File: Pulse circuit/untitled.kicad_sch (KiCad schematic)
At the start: 1 part, among them U4 MP1584EN(SOIC8E)

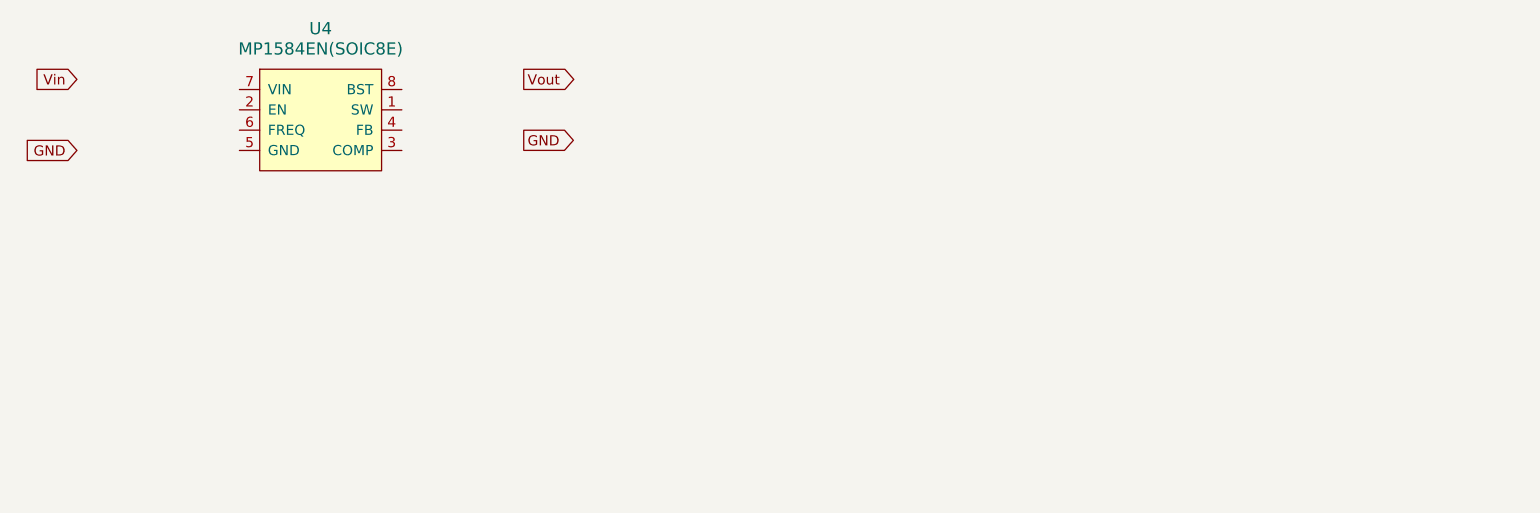
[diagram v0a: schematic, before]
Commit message: schematic of buck converter
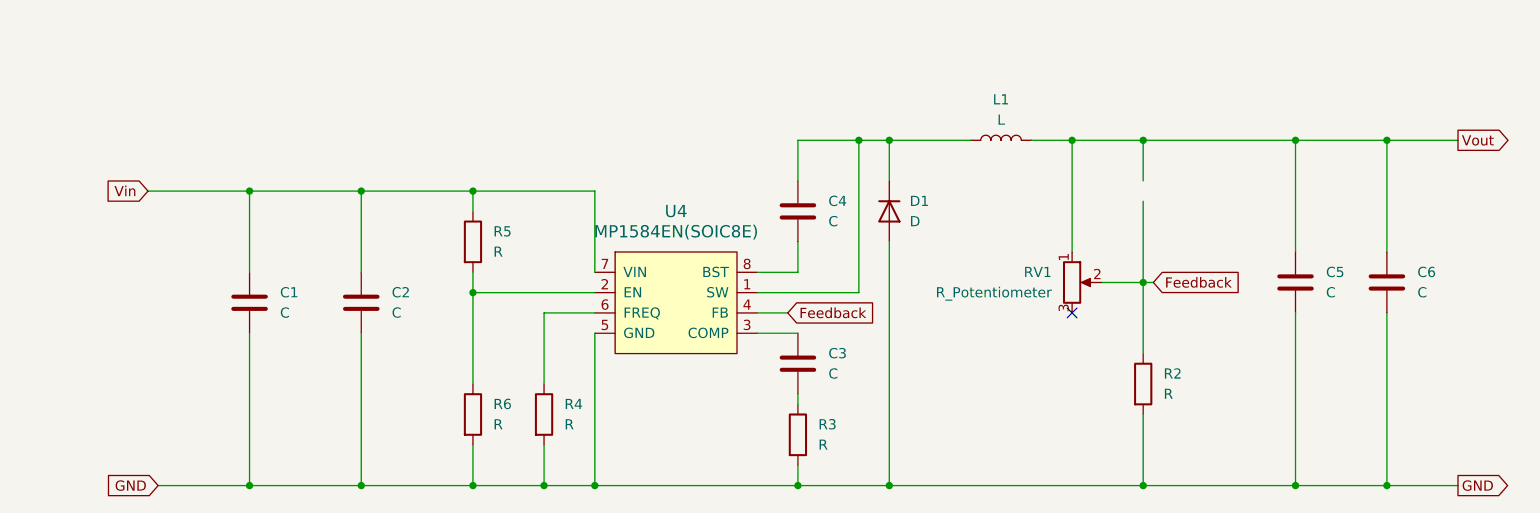
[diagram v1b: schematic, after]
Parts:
- added C1, C2, C3, C4, C5, C6: C, symbol Device:C
- added D1: D, symbol Device:D
- added L1: L, symbol Device:L
- added R2, R3, R4, R5, R6: R, symbol Device:R
- added RV1: R_Potentiometer, symbol Device:R_Potentiometer
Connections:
- net GND: now also U4.5 (GND), U4.EP, U4.EP1 (EP@1), C1.2, C2.2, C5.2, C6.2, D1.2 (A), R2.2, R3.2, R4.2, R6.2
- net Vin: now also U4.7 (VIN), C1.1, C2.1, R5.1
- net Vout: now also C5.1, C6.1, L1.2, RV1.1
- net at U4.1 (SW): now also C4.1, D1.1 (K), L1.1
- net at U4.2 (EN): now also R5.2, R6.1
- net at U4.3 (COMP): now also C3.1
- net Feedback: now reaches U4.4 (FB)
- net Feedback: now also R2.1, RV1.2
- net at U4.6 (FREQ): now also R4.1
- net at U4.8 (BST): now also C4.2
- new net: C3.2, R3.1
- no-connect marks 0 -> 1
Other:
- moved on the sheet: U4

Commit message: Changed the annotations
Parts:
- D1: value D -> ~
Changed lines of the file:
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@@
 			)
 		)
-		(property "Value" "D"
+		(property "Value" "~"
 			(at 162.56 77.4699 90)
 			(effects

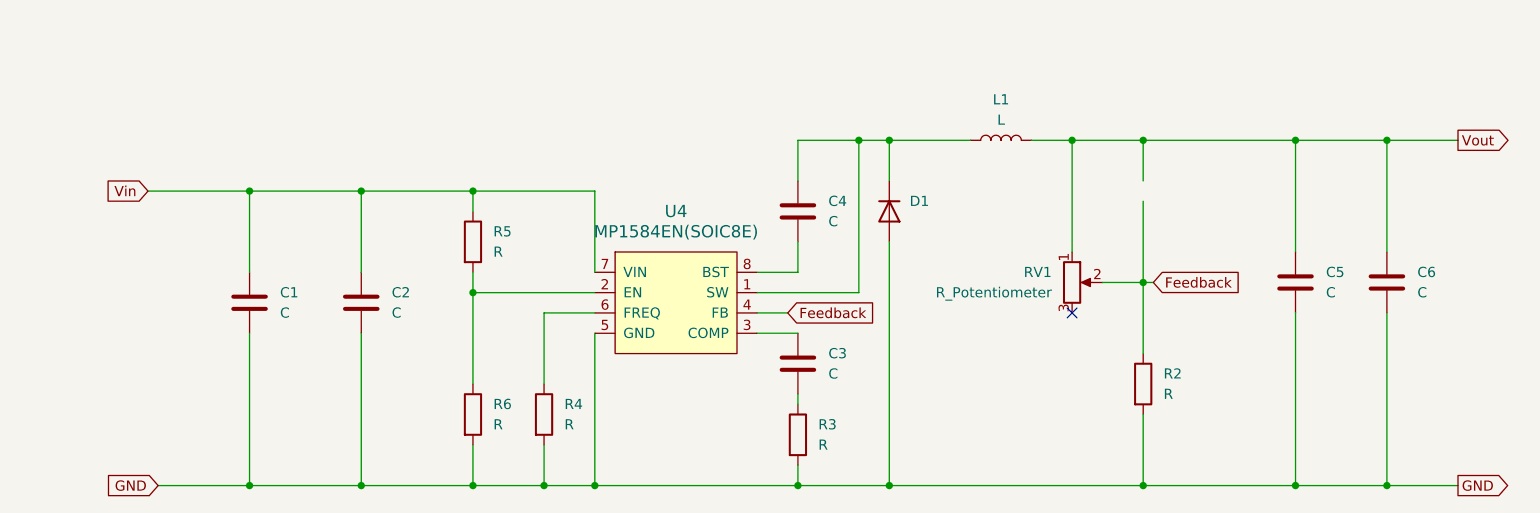
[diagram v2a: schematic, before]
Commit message: values added to buck converter
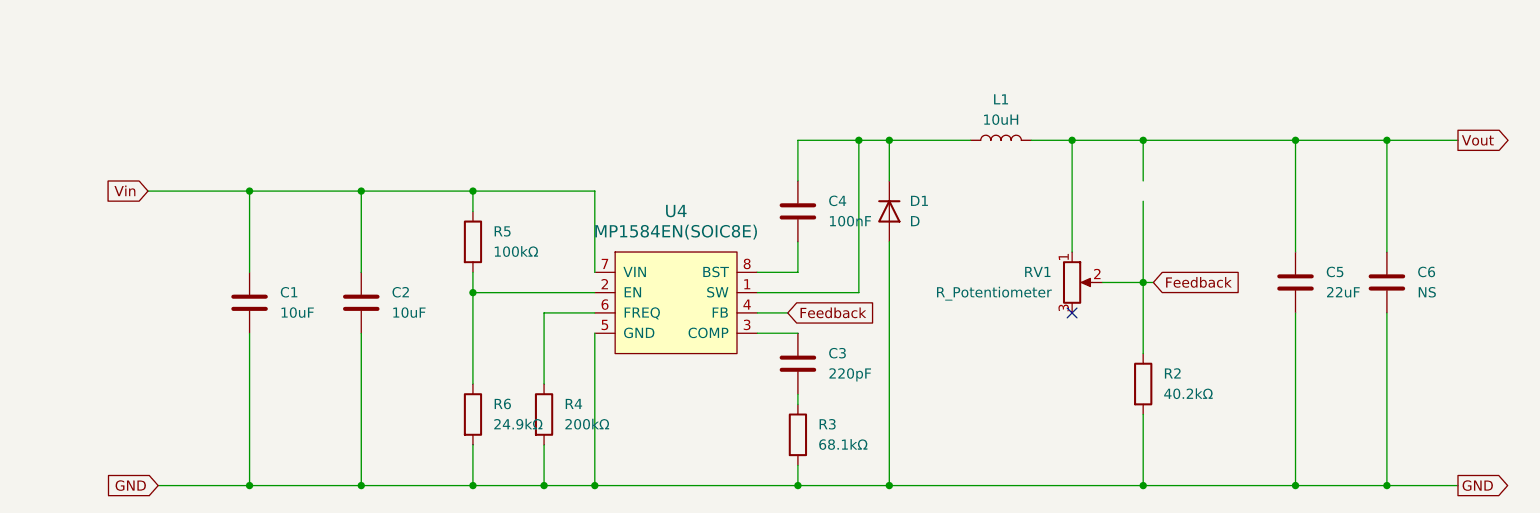
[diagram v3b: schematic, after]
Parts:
- C1, C2: value C -> 10uF
- C3: value C -> 220pF
- C4: value C -> 100nF
- C5: value C -> 22uF
- C6: value C -> NS
- D1: value ~ -> D
- L1: value L -> 10uH
- R2: value R -> 40.2kΩ
- R3: value R -> 68.1kΩ
- R4: value R -> 200kΩ
- R5: value R -> 100kΩ
- R6: value R -> 24.9kΩ
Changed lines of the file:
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@@
 			)
 		)
-		(property "Value" "C"
+		(property "Value" "NS"
 			(at 226.06 86.3599 0)
 			(effects
@@
 			)
 		)
-		(property "Value" "C"
+		(property "Value" "10uF"
 			(at 97.79 88.8999 0)
 			(effects
@@
 			)
 		)
-		(property "Value" "~"
+		(property "Value" "D"
 			(at 162.56 77.4699 90)
 			(effects
@@
 			)
 		)
-		(property "Value" "R"
+		(property "Value" "68.1kΩ"
 			(at 151.13 105.4099 0)
 			(effects
@@
 			)
 		)
-		(property "Value" "C"
+		(property "Value" "100nF"
 			(at 152.4 77.4699 0)
 			(effects
@@
 			)
 		)
-		(property "Value" "R"
+		(property "Value" "100kΩ"
 			(at 110.49 81.2799 0)
 			(effects
@@
 			)
 		)
-		(property "Value" "L"
+		(property "Value" "10uH"
 			(at 173.99 64.77 90)
 			(effects
@@
 			)
 		)
-		(property "Value" "C"
+		(property "Value" "22uF"
 			(at 214.63 86.3599 0)
 			(effects
@@
 			)
 		)
-		(property "Value" "C"
+		(property "Value" "220pF"
 			(at 152.4 96.5199 0)
 			(effects
@@
 			)
 		)
-		(property "Value" "R"
+		(property "Value" "40.2kΩ"
 			(at 194.31 99.0599 0)
 			(effects
@@
 			)
 		)
-		(property "Value" "C"
+		(property "Value" "10uF"
 			(at 83.82 88.8999 0)
 			(effects
@@
 			)
 		)
-		(property "Value" "R"
+		(property "Value" "200kΩ"
 			(at 119.38 102.8699 0)
 			(effects
@@
 			)
 		)
-		(property "Value" "R"
+		(property "Value" "24.9kΩ"
 			(at 110.49 102.8699 0)
 			(effects

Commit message: Added footprints for the resistors
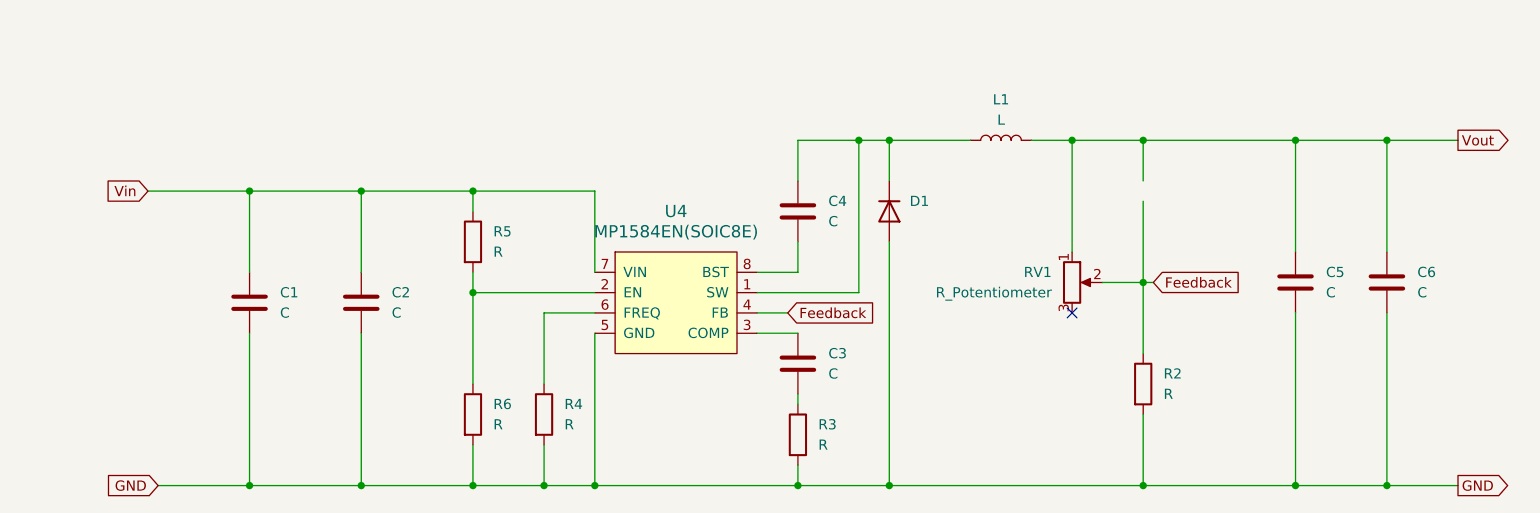
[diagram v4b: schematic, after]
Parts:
- C1, C2: value 10uF -> C
- C3: value 220pF -> C
- C4: value 100nF -> C
- C5: value 22uF -> C
- C6: value NS -> C
- D1: value D -> ~
- L1: value 10uH -> L
- R2: value 40.2kΩ -> R
- R3: value 68.1kΩ -> R
- R4: value 200kΩ -> R
- R5: value 100kΩ -> R
- R6: value 24.9kΩ -> R
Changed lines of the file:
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@@
 			)
 		)
-		(property "Value" "NS"
+		(property "Value" "C"
 			(at 226.06 86.3599 0)
 			(effects
@@
 			)
 		)
-		(property "Value" "10uF"
+		(property "Value" "C"
 			(at 97.79 88.8999 0)
 			(effects
@@
 			)
 		)
-		(property "Value" "D"
+		(property "Value" "~"
 			(at 162.56 77.4699 90)
 			(effects
@@
 			)
 		)
-		(property "Value" "68.1kΩ"
+		(property "Value" "R"
 			(at 151.13 105.4099 0)
 			(effects
@@
 			)
 		)
-		(property "Value" "100nF"
+		(property "Value" "C"
 			(at 152.4 77.4699 0)
 			(effects
@@
 			)
 		)
-		(property "Value" "100kΩ"
+		(property "Value" "R"
 			(at 110.49 81.2799 0)
 			(effects
@@
 			)
 		)
-		(property "Value" "10uH"
+		(property "Value" "L"
 			(at 173.99 64.77 90)
 			(effects
@@
 			)
 		)
-		(property "Value" "22uF"
+		(property "Value" "C"
 			(at 214.63 86.3599 0)
 			(effects
@@
 			)
 		)
-		(property "Value" "220pF"
+		(property "Value" "C"
 			(at 152.4 96.5199 0)
 			(effects
@@
 			)
 		)
-		(property "Value" "40.2kΩ"
+		(property "Value" "R"
 			(at 194.31 99.0599 0)
 			(effects
@@
 			)
 		)
-		(property "Value" "10uF"
+		(property "Value" "C"
 			(at 83.82 88.8999 0)
 			(effects
@@
 			)
 		)
-		(property "Value" "200kΩ"
+		(property "Value" "R"
 			(at 119.38 102.8699 0)
 			(effects
@@
 			)
 		)
-		(property "Value" "24.9kΩ"
+		(property "Value" "R"
 			(at 110.49 102.8699 0)
 			(effects
